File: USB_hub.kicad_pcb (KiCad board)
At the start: 6 copper layers, 119.5 x 91.8 mm, 308 parts, among them J1 USB_SPI_(Opt), J10 USB3_A, J11 8-pin ATX connector, J12 USB_C_Receptacle, J13 I2C_HD3SS3220, J2 USB_C_Receptacle, J3 I2C_HD3SS3220, J4 USB_C_Receptacle, J5 I2C2_PD_Controller, J6 I2C_Mux, J7 I2C_EEPROM, J8 SD_Card_Receptacle, J9 USB3_A, Q1 MMBT2222A, SW1 RESET_HUB, SW2 FW_Upgrade, U1 USB7206C/KDX, U10 24LC256, U11 TPD4E02B04DQA, U12 TPD4E02B04DQA, U13 TPD4E02B04DQA, U14 TUSB1142IRNQR_C5216209, U15 GL3224-OIY04, U16 TPD4E02B04DQA, U17 TPD4E02B04DQA, U18 UCS2114-1-V/G4, U19 TPD4E02B04DQA, U2 MIC803-29D4VM3-TR, U20 TPD4E02B04DQA, U21 SiRA80DP, U22 TPS25983, U23 AP7361C-33E, U24 MP8795, U25 MIC23201YML-TR, U26 HD3SS3220IRNHR, U27 TPD4E02B04DQA, U28 TPD4E02B04DQA, U29 TPD4E02B04DQA, U3 HD3SS3220IRNHR, U32 TPD4E02B04DQA, U4 TPS2068EDBVR, U5 TPD4E02B04DQA, U6 TPD4E02B04DQA, U7 TPD4E02B04DQA, U8 TVS2200DRV, U9 TPS25762CQRQLRQ1, Y1 25MHz, Y2 25MHz +-0.03%

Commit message: Added lcsc part number for most of components, fixes for better routing
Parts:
- added C127: 100nF, Capacitor_SMD:C_0402_1005Metric, F.Cu at (236.2, -145.2)
- added C128: 100nF, Capacitor_SMD:C_0402_1005Metric, F.Cu at (234.7, -145.2)
- added C129: 100nF, Capacitor_SMD:C_0402_1005Metric, F.Cu at (246.9, -152.8)
- added C130: 100nF, Capacitor_SMD:C_0402_1005Metric, F.Cu at (245.3, -152.8)
- C1, C11, C12, C13, C14, C15, C16, C17, C18, C2, C3, C4, C5, C6, C7, C8, C86, C9, C92, C94: value 0.1u -> 0.1uF
- C10, C19: value 4.7u -> 4.7uF; footprint Capacitor_SMD:C_0402_1005Metric -> Capacitor_SMD:C_0805_2012Metric
- C100, C101, C47, C95, C99: footprint Capacitor_SMD:C_0402_1005Metric -> Capacitor_SMD:C_0603_1608Metric
- C102, C20, C96, C97, C98: footprint Capacitor_SMD:C_0402_1005Metric -> Capacitor_SMD:C_0805_2012Metric
- C105, C85, C91, C93: value 1u -> 1uF; footprint Capacitor_SMD:C_0402_1005Metric -> Capacitor_SMD:C_0603_1608Metric
- C106, C107, C108, C109, C110, C111, C114, C117: footprint Capacitor_SMD:C_0402_1005Metric -> Capacitor_THT:C_Radial_D5.0mm_H11.0mm_P2.00mm
- C121, C23, C29, C31: footprint Capacitor_THT:C_Radial_D10.0mm_H16.0mm_P5.00mm -> Capacitor_THT:C_Radial_D6.3mm_H11.0mm_P2.50mm
- C21, C22, C78, C79: value C -> 18pF
- C38, C50, C80, C81, C82, C83: footprint Capacitor_THT:C_Radial_D10.0mm_H16.0mm_P5.00mm -> Capacitor_THT:C_Radial_D5.0mm_H11.0mm_P2.00mm
- C51: value 90uF (50V) -> 100uF (50V); footprint Capacitor_THT:C_Radial_D10.0mm_H16.0mm_P5.00mm -> Capacitor_THT:C_Radial_D6.3mm_H11.0mm_P2.50mm
- C65: footprint Capacitor_THT:C_Radial_D10.0mm_H16.0mm_P5.00mm -> Capacitor_SMD:C_0805_2012Metric
- C90: value 4.3nF -> 4.7nF
- D3: value LED -> RED
- D5: footprint Diode_SMD:D_0603_1608Metric -> LED_SMD:LED_0603_1608Metric
- L1: value 4.7uF -> 4.7uH; footprint Inductor_SMD:L_6.3x6.3_H3 -> Inductor_SMD:L_Coilcraft_XAL1010-XXX
- R27: value 10 (0.1W) -> 10 (0.1W); footprint Resistor_SMD:R_0402_1005Metric -> Resistor_SMD:R_0603_1608Metric
- R29: value 10 0.25W -> 10 (0.25W); footprint Resistor_SMD:R_0402_1005Metric -> Resistor_SMD:R_0603_1608Metric
- R31: footprint Resistor_SMD:R_0402_1005Metric -> Resistor_SMD:R_0603_1608Metric
- R32: footprint Resistor_SMD:R_1206_3216Metric -> Resistor_SMD:R_2010_5025Metric
- SW1, SW2: moved to B.Cu
- U23: value AP7361C-33E -> AP7361C-33ER
- Y1, Y2: footprint Crystal:Crystal_SMD_0603-4Pin_6.0x3.5mm -> Crystal:Crystal_SMD_3225-4Pin_3.2x2.5mm
- moved C51 462.5 mm to (304.4, -177.9), turned to 90 degrees
- moved TP3 460.0 mm to (324.5, -202.4)
- moved TP4 460.0 mm to (324.5, -197.8)
- moved D16 444.8 mm to (182.1, -157.2), turned to 90 degrees
- moved R85 443.1 mm to (183.0, -159.9), turned to 180 degrees
- moved SW2 439.3 mm to (336.5, -171.6), turned to 180 degrees
- moved C47 438.6 mm to (330.4, -172.0)
- moved R29 437.9 mm to (328.1, -171.2)
- moved R28 437.9 mm to (328.1, -169.9)
- moved C45 437.9 mm to (328.1, -172.5)
- moved J6 420.6 mm to (364.5, -188.3)
- moved J7 420.6 mm to (368.6, -188.3)
- moved U13 420.6 mm to (406.9, -189.4)
- moved J3 420.6 mm to (397.2, -162.6)
- moved TP1 420.6 mm to (390.5, -155.8)
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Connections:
- C50 pad 1: Net-(C50-Pad1) -> Net-(U9-OUT)
- D2 pad 1: VBUS-C1 -> VBUS_C1
- R31 pad 2: Net-(C50-Pad1) -> Net-(U9-OUT)
- R32 pad 2: Net-(C50-Pad1) -> Net-(U9-OUT)
- R85 pad 1: +5V -> +5V_prefiltered
- U1 pad 16: /USB-A1/USB-A2.TX1+ -> Net-(U1-USB3DN_TXDP2)
- U1 pad 17: /USB-A1/USB-A2.TX1- -> Net-(U1-USB3DN_TXDM2)
- U1 pad 29: /USB-A1/USB-A1.TX1+ -> Net-(U1-USB3DN_TXDP3)
- U1 pad 30: /USB-A1/USB-A1.TX1- -> Net-(U1-USB3DN_TXDM3)
- U1 pad 57: /USB-A1/PRT_EN1 -> unconnected-(U1-PRT_CTL4/PF14-Pad57)
- U1 pad 58: /USB-A1/PRT_EN2 -> /USB-A1/PRT_EN1
- U1 pad 59: unconnected-(U1-PRT_CTL2/PF16-Pad59) -> /USB-A1/PRT_EN2
- U16 pad 1: /SD-interface/SD_D0 -> /SD-interface/SD_CD
- U16 pad 10: /SD-interface/SD_D0 -> /SD-interface/SD_CD
- U16 pad 2: /SD-interface/SD_D1 -> /SD-interface/SD_CM
- U16 pad 4: /SD-interface/SD_D2 -> /SD-interface/SD_D3
- U16 pad 5: /SD-interface/SD_D3 -> /SD-interface/SD_D2
- U16 pad 6: /SD-interface/SD_D3 -> /SD-interface/SD_D2
- U16 pad 7: /SD-interface/SD_D2 -> /SD-interface/SD_D3
- U16 pad 9: /SD-interface/SD_D1 -> /SD-interface/SD_CM
- U17 pad 1: /SD-interface/SD_CK -> /SD-interface/SD_WP
- U17 pad 10: /SD-interface/SD_CK -> /SD-interface/SD_WP
- U17 pad 2: /SD-interface/SD_CM -> /SD-interface/SD_D1
- U17 pad 4: /SD-interface/SD_CD -> /SD-interface/SD_D0
- U17 pad 5: /SD-interface/SD_WP -> /SD-interface/SD_CK
- U17 pad 6: /SD-interface/SD_WP -> /SD-interface/SD_CK
- U17 pad 7: /SD-interface/SD_CD -> /SD-interface/SD_D0
- U17 pad 9: /SD-interface/SD_CM -> /SD-interface/SD_D1
- U23 pad 1: +5V_Power -> GND
- U23 pad 2: GND -> +3V3
- U23 pad 3: +3V3 -> +5V_Power
- Y1 pad 3: GND -> /USB7206C/XTALO
- Y1 pad 4: /USB7206C/XTALO -> GND
- Y2 pad 3: GND -> /SD-interface/XOUT
- Y2 pad 4: /SD-interface/XOUT -> GND
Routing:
- net Net-(U9-BOOT1): track 0.00 -> 9.85 mm
- net Net-(U9-BOOT2): track 0.00 -> 9.65 mm
- net VCORE: track 5.21 -> 13.6 mm
- net /SD-interface/SD_CK: track 12.6 -> 20.5 mm
- net Net-(U9-OUT): track 0.00 -> 7.47 mm
- net /USB-A1/USB-A1.RX1-: track 0.00 -> 6.40 mm
- net /USB-A1/USB-A1.RX1+: track 0.00 -> 6.40 mm
- net Net-(U9-EN/UVLO): track 0.00 -> 6.07 mm
- net /SD-interface/SD_WP: track 0.00 -> 6.02 mm
- net +3V3_LDO: track 0.00 -> 5.44 mm
- net +5V_LDO: track 0.00 -> 4.84 mm
- net Net-(U9-SW2): track 0.00 -> 4.64 mm
- net Net-(U9-SW1): track 0.00 -> 4.63 mm
- net Net-(U9-CSN/BUS): track 0.00 -> 4.37 mm
- net /USB-C2/I2C2_TPS.SCL: track 0.00 -> 4.33 mm
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
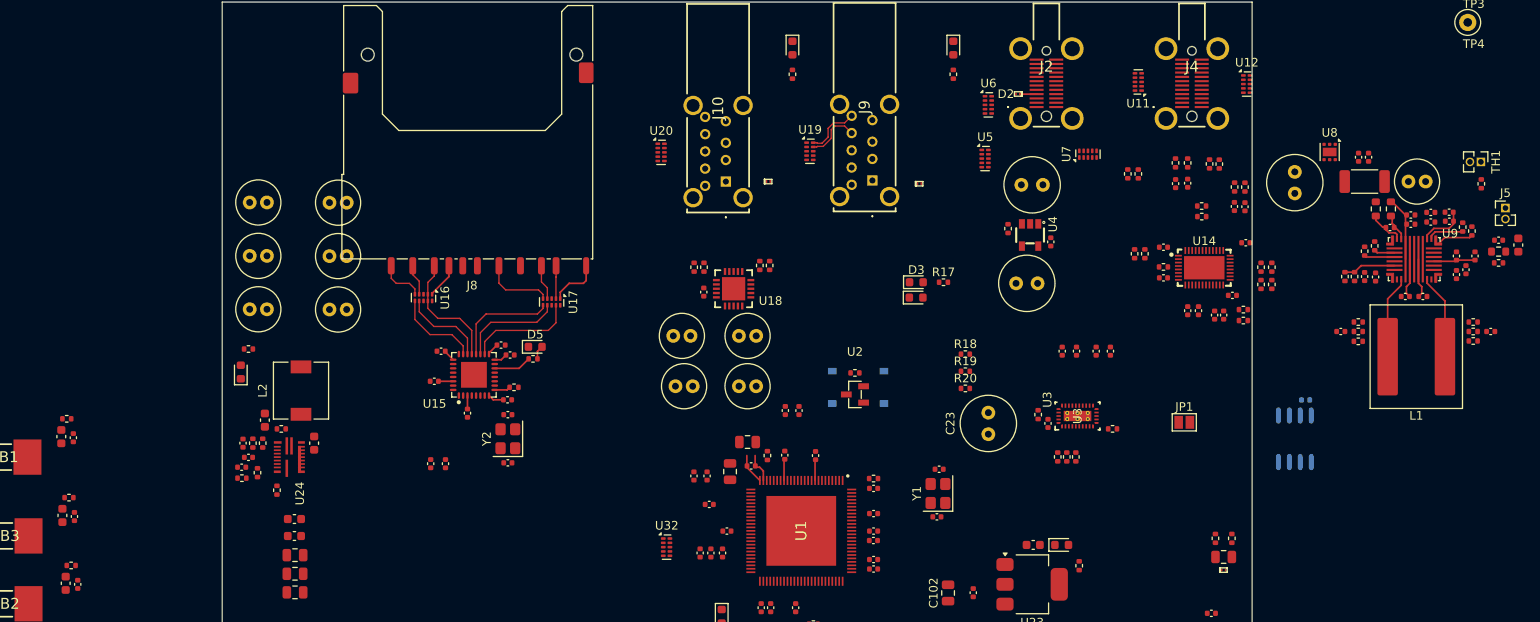
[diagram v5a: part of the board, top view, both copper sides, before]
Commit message: Added lcsc part number for most of resistors
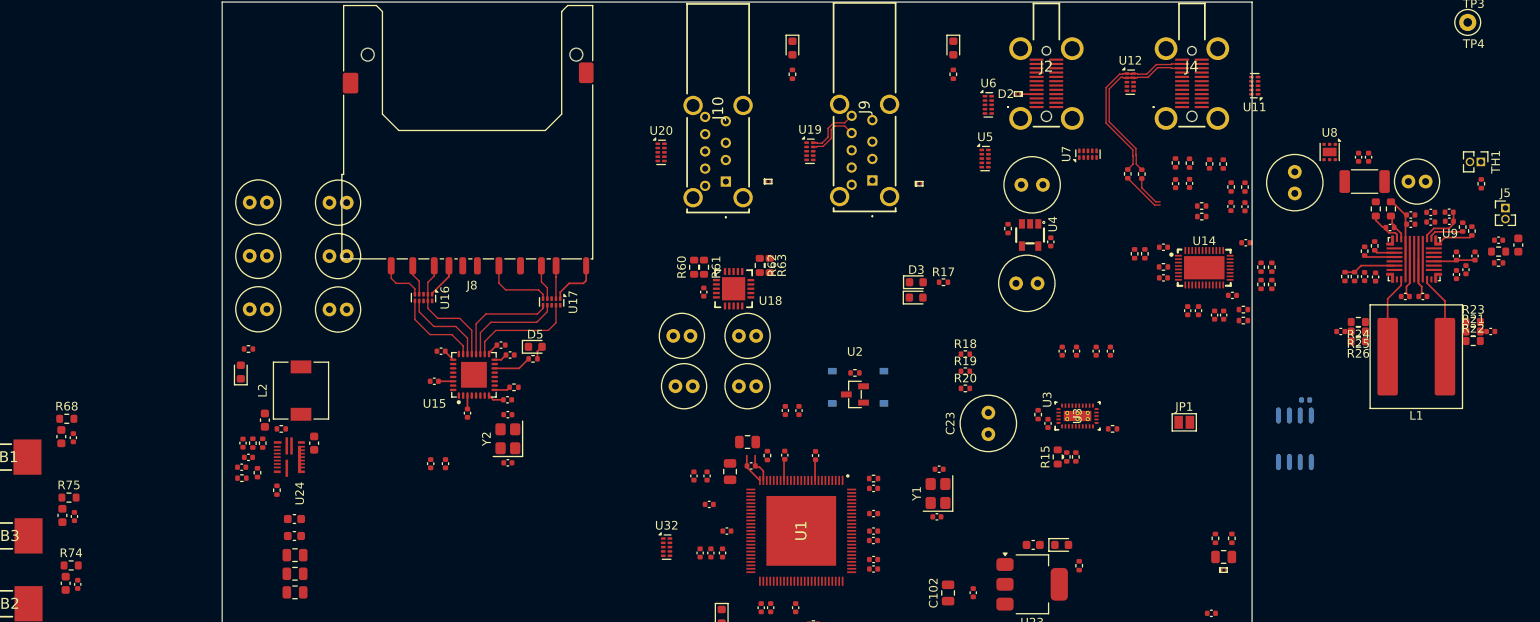
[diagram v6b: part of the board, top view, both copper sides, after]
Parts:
- R15, R21, R22, R23, R24, R25, R26, R60, R61, R62, R63, R68, R74, R75: footprint Resistor_SMD:R_0402_1005Metric -> Resistor_SMD:R_0603_1608Metric
- R39: value 1k DNP -> 1k
- R59: value 520 -> 560
- moved U11 13.5 mm to (299.8, -190.4)
- moved U12 13.5 mm to (285.3, -190.9)
- moved R53 0.46 mm to (296.1, -181.4)
- moved R47 0.41 mm to (286.7, -180.2)
- moved R41 0.41 mm to (297.0, -178.7)
- moved C57 0.41 mm to (297.0, -176.4)
- moved C60 0.22 mm to (292.2, -179.1)
- moved R49 0.22 mm to (292.2, -181.5)
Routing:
- net /USB-C2/USB-C2.RX2+: track 0.00 -> 21.1 mm
- net /USB-C2/USB-C2.RX2-: track 0.00 -> 20.6 mm
- net /USB-C2/CRX2+: track 0.00 -> 5.04 mm
- net /USB-C2/CRX2-: track 0.00 -> 3.89 mm

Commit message: minor schematic fixes, footprints changes, layout improvements
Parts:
- removed TP11: Out1, TestPoint:TestPoint_Loop_D1.80mm_Drill1.0mm_Beaded
- removed TP12: Out2, TestPoint:TestPoint_Loop_D1.80mm_Drill1.0mm_Beaded
- C114, C117: footprint Capacitor_THT:C_Radial_D5.0mm_H11.0mm_P2.00mm -> Capacitor_SMD:C_1812_4532Metric
- C121, C23: footprint Capacitor_THT:C_Radial_D6.3mm_H11.0mm_P2.50mm -> Capacitor_SMD:C_0805_2012Metric
- C25, C26, C32, C33, C34, C35, C36, C37, C39, C40, C41, C42, C43, C44, C45, C46, C47, C48, C49, C51, C52, C53, C54, C55, C65, J5, L1, NT1, R21, R22, R23, R24, R25, R26, R27, R28, R29, R30, R31, R32, R33, R34, R35, R36, R37, R38, TH1, U19, U20, U8, U9: moved to B.Cu
- C38: footprint Capacitor_THT:C_Radial_D5.0mm_H11.0mm_P2.00mm -> Capacitor_SMD:C_1812_4532Metric; moved to B.Cu
- C50: value 30uF (50V) -> 33uF (50V); footprint Capacitor_THT:C_Radial_D5.0mm_H11.0mm_P2.00mm -> Capacitor_SMD:C_2220_5750Metric; moved to B.Cu
- L2: value 4.7nH -> 4.7uH; footprint Inductor_SMD:L_6.3x6.3_H3 -> Inductor_SMD:L_Coilcraft_XAL1010-XXX
- L3: value 1.5u -> 1.5uH
- R81: value 8.2k -> 8k; footprint Resistor_SMD:R_0402_1005Metric -> Resistor_SMD:R_0603_1608Metric
- SW1: footprint Button_Switch_SMD:SW_Push_1P1T_XKB_TS-1187A -> EasyEDA:ultra_small_switch_1.6x3.0mm; moved to F.Cu
- SW2: footprint Button_Switch_SMD:SW_Push_1P1T_XKB_TS-1187A -> EasyEDA:ultra_small_switch_1.6x3.0mm
- TP1, TP10, TP2, TP3, TP4, TP5, TP6, TP7, TP8, TP9: footprint TestPoint:TestPoint_Loop_D1.80mm_Drill1.0mm_Beaded -> TestPoint:TestPoint_Pad_D1.0mm
- moved U13 318.5 mm to (172.8, 26.6)
- moved R9 317.2 mm to (128.9, 64.0), turned to 180 degrees
- moved R7 315.3 mm to (128.9, 62.9), turned to 180 degrees
- moved J3 312.6 mm to (156.4, 36.8), turned to 180 degrees
- moved TP1 307.0 mm to (154.1, 40.0)
- moved J6 305.7 mm to (181.2, 56.4)
- moved J7 305.7 mm to (185.4, 56.4)
- moved TP2 305.4 mm to (154.1, 42.1)
- moved SW2 293.7 mm to (154.9, 59.2), turned to -90 degrees
- moved C47 288.3 mm to (156.9, 58.3)
- moved TH1 288.3 mm to (175.0, 64.0)
- moved J5 285.8 mm to (158.1, 52.9), turned to 180 degrees
- moved R28 285.6 mm to (159.2, 60.4), turned to 180 degrees
- moved R29 285.6 mm to (159.2, 59.1), turned to 180 degrees
- moved C45 285.6 mm to (159.2, 57.8), turned to 180 degrees
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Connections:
- net Net-(U3-TX1N) renamed /USB-C1/TX1-
- net Net-(U3-TX1P) renamed /USB-C1/TX1+
- net Net-(U3-TX2N) renamed /USB-C1/TX2-
- net Net-(U3-TX2P) renamed /USB-C1/TX2+
- C42 pad 2: Net-(U9-SW2) -> Net-(U9-BOOT2)
- C44 pad 2: Net-(U9-SW1) -> Net-(U9-BOOT1)
- J2 pad A2: /USB-C1/USB-C1.TX1+ -> /USB-C1/USB-C1.TX1-
- J2 pad A3: /USB-C1/USB-C1.TX1- -> /USB-C1/USB-C1.TX1+
- J2 pad B2: /USB-C1/USB-C1.TX2+ -> /USB-C1/USB-C1.TX2-
- J2 pad B3: /USB-C1/USB-C1.TX2- -> /USB-C1/USB-C1.TX2+
- L1 pad 1: Net-(U9-BOOT1) -> Net-(U9-SW1)
- L1 pad 2: Net-(U9-BOOT2) -> Net-(U9-SW2)
- R21 pad 1: Net-(U9-BOOT1) -> Net-(U9-SW1)
- R22 pad 1: Net-(U9-BOOT1) -> Net-(U9-SW1)
- R23 pad 1: Net-(U9-BOOT1) -> Net-(U9-SW1)
- R24 pad 1: Net-(U9-BOOT2) -> Net-(U9-SW2)
- R25 pad 1: Net-(U9-BOOT2) -> Net-(U9-SW2)
- R26 pad 1: Net-(U9-BOOT2) -> Net-(U9-SW2)
- R60 pad 2: /USB-A1/PRT_EN1 -> /USB-A1/PRT_EN2
- R63 pad 1: /USB-A1/PRT_EN2 -> /USB-A1/PRT_EN1
- U1 pad 91: /USB-C_UP1/USB3_IN.TX1+ -> /USB-C_UP1/USB3_IN.TX1-
- U1 pad 92: /USB-C_UP1/USB3_IN.TX1- -> /USB-C_UP1/USB3_IN.TX1+
- U1 pad 94: /USB-C_UP1/USB3_IN.RX1+ -> /USB-C_UP1/USB3_IN.RX1-
- U1 pad 95: /USB-C_UP1/USB3_IN.RX1- -> /USB-C_UP1/USB3_IN.RX1+
- U12 pad 4: /USB-C2/USB-C2.TX1- -> /USB-C2/USB3_IN.D-
- U12 pad 5: /USB-C2/USB-C2.TX1+ -> /USB-C2/USB3_IN.D+
- U12 pad 6: /USB-C2/USB-C2.TX1+ -> /USB-C2/USB3_IN.D+
- U12 pad 7: /USB-C2/USB-C2.TX1- -> /USB-C2/USB3_IN.D-
- U13 pad 4: /USB-C2/USB3_IN.D- -> /USB-C2/USB-C2.TX1-
- U13 pad 5: /USB-C2/USB3_IN.D+ -> /USB-C2/USB-C2.TX1+
- U13 pad 6: /USB-C2/USB3_IN.D+ -> /USB-C2/USB-C2.TX1+
- U13 pad 7: /USB-C2/USB3_IN.D- -> /USB-C2/USB-C2.TX1-
- U18 pad 11: VBUS-A2 -> VBUS-A1
- U18 pad 12: VBUS-A2 -> VBUS-A1
- U18 pad 4: VBUS-A1 -> VBUS-A2
- U18 pad 5: VBUS-A1 -> VBUS-A2
- U5 pad 4: /USB-C1/USB-C1.D- -> /USB-C1/USB-C1.TX1+
- U5 pad 5: /USB-C1/USB-C1.D+ -> /USB-C1/USB-C1.TX1-
- U5 pad 6: /USB-C1/USB-C1.D+ -> /USB-C1/USB-C1.TX1-
- U5 pad 7: /USB-C1/USB-C1.D- -> /USB-C1/USB-C1.TX1+
- U6 pad 4: /USB-C1/USB-C1.TX1- -> /USB-C1/USB3_IN.D-
- U6 pad 5: /USB-C1/USB-C1.TX1+ -> /USB-C1/USB3_IN.D+
- U6 pad 6: /USB-C1/USB-C1.TX1+ -> /USB-C1/USB3_IN.D+
- U6 pad 7: /USB-C1/USB-C1.TX1- -> /USB-C1/USB3_IN.D-
- U7 pad 4: /USB-C1/USB-C1.TX2- -> /USB-C1/USB-C1.TX2+
- U7 pad 5: /USB-C1/USB-C1.TX2+ -> /USB-C1/USB-C1.TX2-
- U7 pad 6: /USB-C1/USB-C1.TX2+ -> /USB-C1/USB-C1.TX2-
- U7 pad 7: /USB-C1/USB-C1.TX2- -> /USB-C1/USB-C1.TX2+
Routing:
- net /USB-C2/USB3_IN.TX1+: track 0.00 -> 61.5 mm
- net /USB-C2/USB3_IN.TX1-: track 0.00 -> 60.9 mm
- net /USB-C2/USB3_IN.RX1+: track 0.00 -> 59.8 mm, vias 0 -> 1
- net /USB-C2/USB3_IN.RX1-: track 0.00 -> 59.3 mm, vias 0 -> 1
- net /USB-C_UP1/USB3_IN.RX1-: track 0.00 -> 44.9 mm, vias 0 -> 2
- net /USB-C_UP1/USB3_IN.RX1+: track 0.00 -> 44.9 mm, vias 0 -> 2
- net /USB-C_UP1/USB3_IN.TX1-: track 0.00 -> 42.5 mm, vias 0 -> 2
- net /USB-C_UP1/USB3_IN.TX1+: track 0.00 -> 42.4 mm, vias 0 -> 2
- net /USB-C1/USB-C1.RX2+: track 0.00 -> 28.8 mm, vias 0 -> 2
- net /USB-C1/USB-C1.TX2-: track 0.00 -> 28.5 mm
- net /USB-C1/USB-C1.TX2+: track 0.00 -> 28.3 mm
- net /USB-C1/USB-C1.RX2-: track 0.00 -> 28.2 mm, vias 0 -> 2
- net /USB-C2/USB-C2.RX2+: track 21.1 -> 0.00 mm
- net /USB-C2/USB-C2.RX2-: track 20.6 -> 0.00 mm
- net /USB-C1/USB-C1.CC2: track 0.00 -> 18.7 mm, vias 0 -> 2
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- added copper zone on In1.Cu, net GND
- added copper zone on In4.Cu, net GND
- added copper zone on In2.Cu, net VCORE
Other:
- board size 119.5 x 91.8 mm -> 121.3 x 91.8 mm

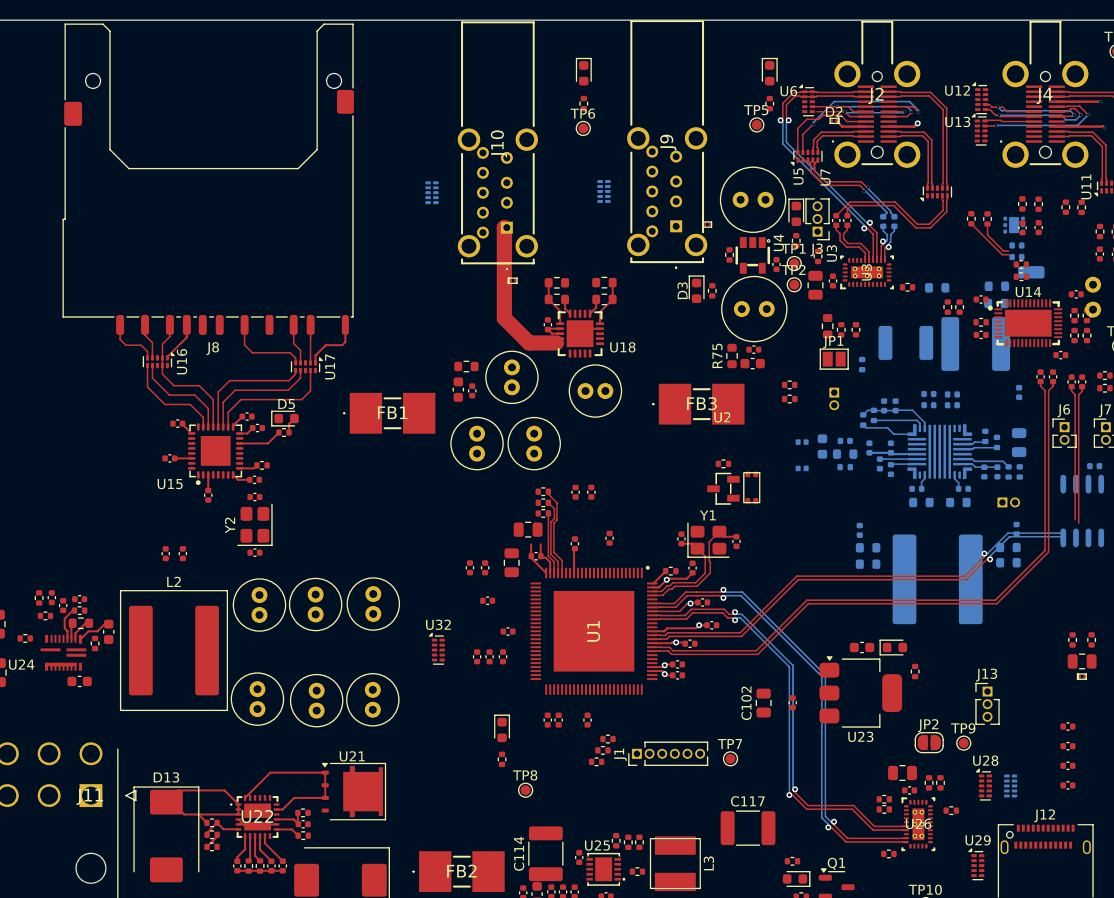
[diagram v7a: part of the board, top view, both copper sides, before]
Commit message: comments to schematic added, changed a few components
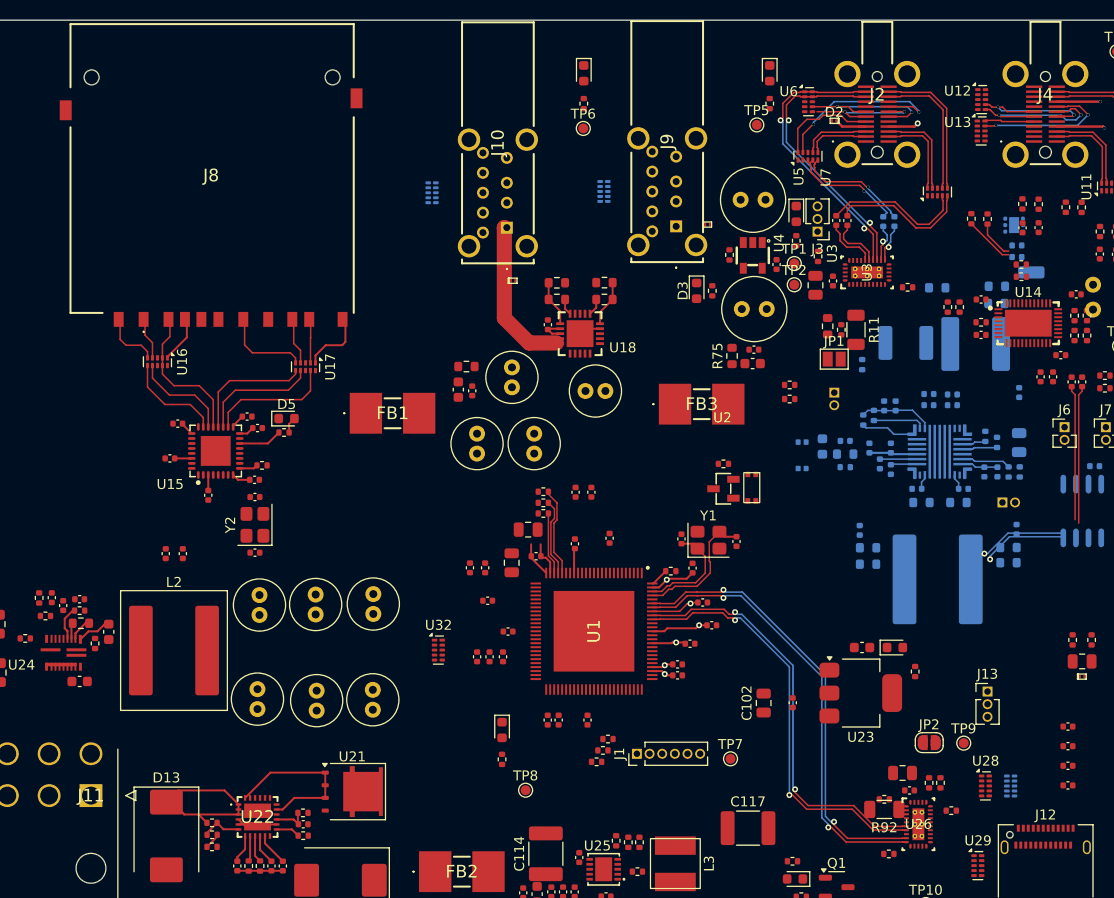
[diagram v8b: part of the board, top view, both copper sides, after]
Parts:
- J8: footprint Connector_Card:SD_Kyocera_145638009511859+ -> SamacSys_Parts:SD2A
- R11, R92: footprint Resistor_SMD:R_0402_1005Metric -> Resistor_SMD:R_1206_3216Metric
- moved J8 2.52 mm to (95.5, 31.1)
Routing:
- net /USB-C2/USB3_IN.TX1+: track 61.5 -> 0.00 mm
- net /USB-C2/USB3_IN.TX1-: track 60.9 -> 0.00 mm
- net /USB-C2/USB3_IN.RX1+: track 59.8 -> 22.5 mm
- net /USB-C2/USB3_IN.RX1-: track 59.3 -> 22.3 mm
